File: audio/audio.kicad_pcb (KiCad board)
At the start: 2 copper layers, 64 x 64 mm, 62 parts, among them J1 Conn_01x02, J2 Conn_01x03, J3 Conn_01x05, U1 LM324DT, U2 LM324DT

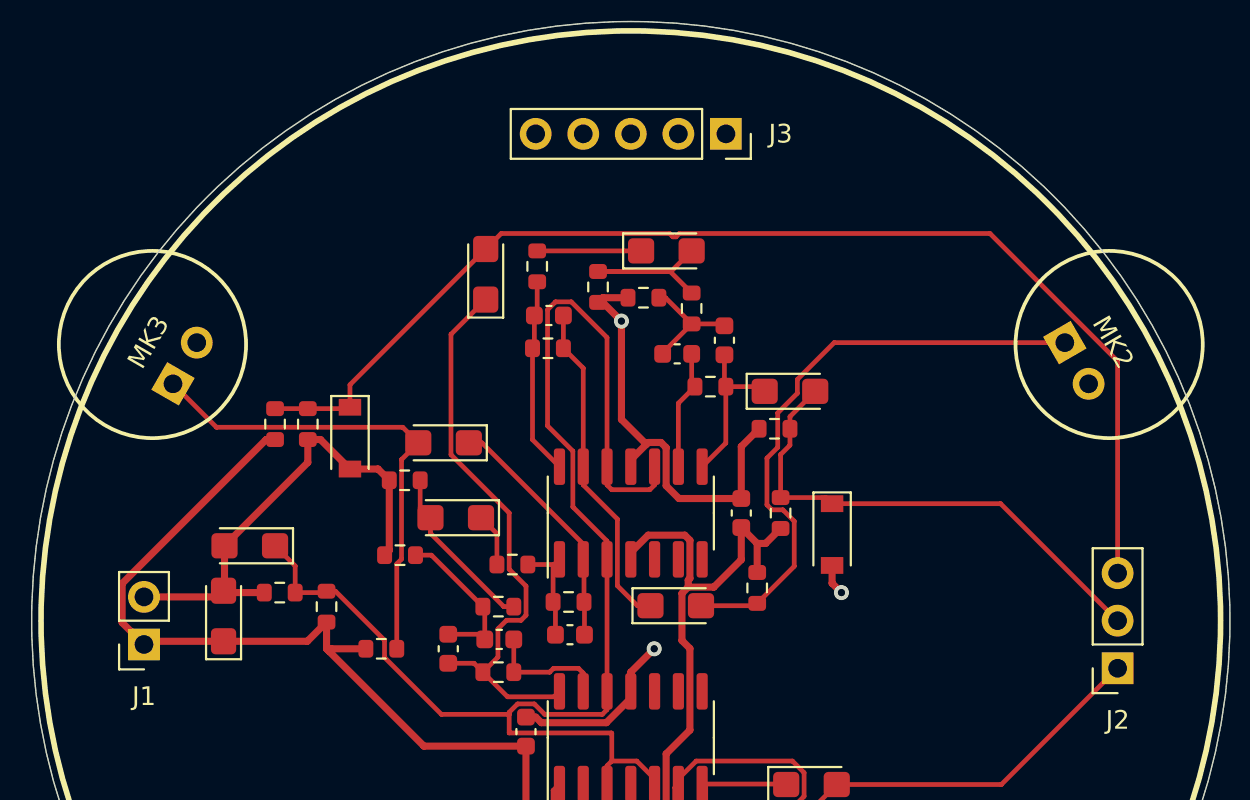
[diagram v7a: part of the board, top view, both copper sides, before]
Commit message: errata 2: fix footprints
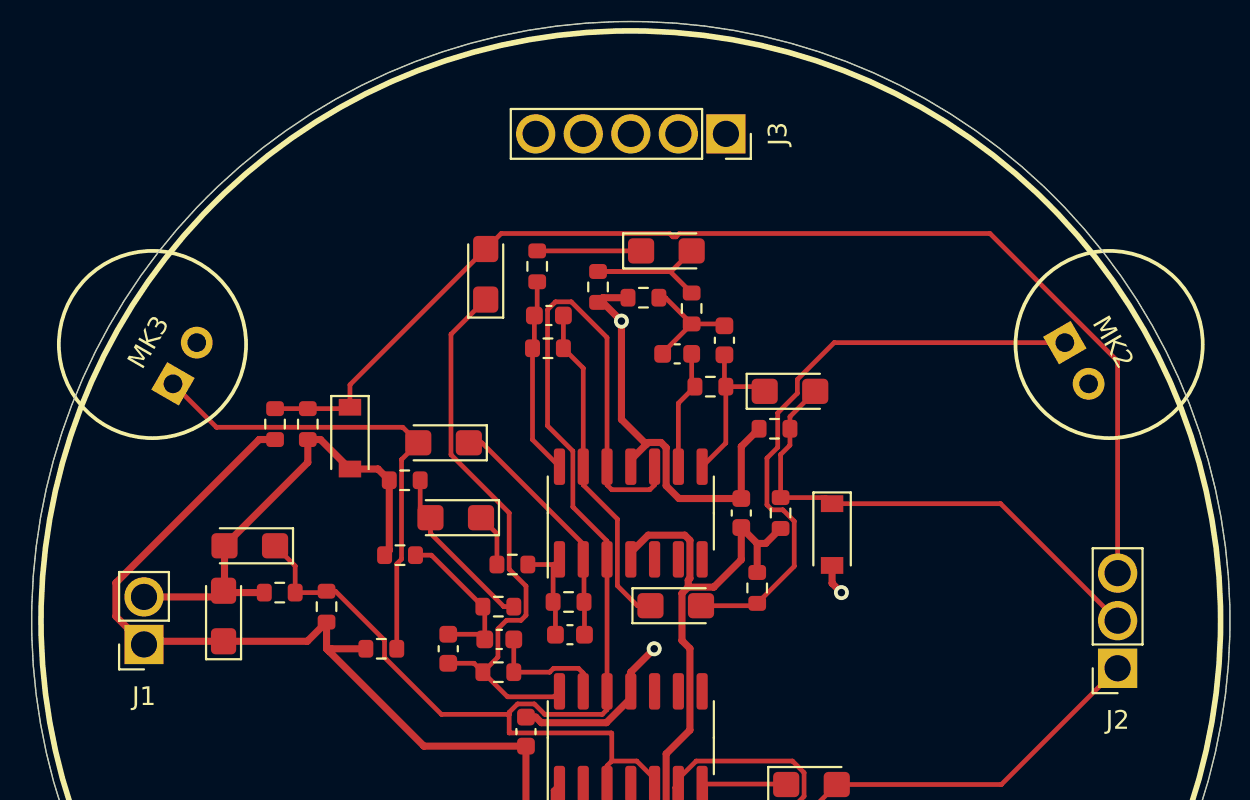
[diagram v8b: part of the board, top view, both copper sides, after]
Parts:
- J1: footprint Connector_PinSocket_2.54mm:PinSocket_1x02_P2.54mm_Vertical -> df-parts:310-XX-102-41-001000
- J2: footprint Connector_PinSocket_2.54mm:PinSocket_1x03_P2.54mm_Vertical -> df-parts:310-XX-103-41-001000
- J3: footprint Connector_PinSocket_2.54mm:PinSocket_1x05_P2.54mm_Vertical -> df-parts:310-XX-105-41-001000
